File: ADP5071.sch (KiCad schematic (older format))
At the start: 29 parts, among them P7 PIN, P8 POUT, T1 NET-TIE, U4 ADP5071

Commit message: Latest power stuff
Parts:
- P7: footprint Pin_Headers:Pin_Header_Angled_1x02 -> Pin_Headers:Pin_Header_Straight_1x02
- P8: footprint Pin_Headers:Pin_Header_Angled_1x03 -> Pin_Headers:Pin_Header_Straight_1x03
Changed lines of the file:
@@
 F 0 "P7" H 2000 2900 50  0000 C CNN
 F 1 "PIN" V 2100 2750 50  0000 C CNN
-F 2 "Pin_Headers:Pin_Header_Angled_1x02" H 2000 2750 60  0001 C CNN
+F 2 "Pin_Headers:Pin_Header_Straight_1x02" H 2000 2750 60  0001 C CNN
 F 3 "" H 2000 2750 60  0000 C CNN
 	1    2000 2750
@@
 F 0 "P8" H 9800 3500 50  0000 C CNN
 F 1 "POUT" V 9900 3300 50  0000 C CNN
-F 2 "Pin_Headers:Pin_Header_Angled_1x03" H 9800 3300 60  0001 C CNN
+F 2 "Pin_Headers:Pin_Header_Straight_1x03" H 9800 3300 60  0001 C CNN
 F 3 "" H 9800 3300 60  0000 C CNN
 	1    9800 3300

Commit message: Latest work
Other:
- moved on the sheet: C19, C20, R8
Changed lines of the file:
@@
 L R R8
 U 1 1 56322611
-P 3700 3800
-F 0 "R8" V 3780 3800 50  0000 C CNN
-F 1 "5.23k" V 3600 3800 50  0000 C CNN
-F 2 "smd:SM0603" V 3630 3800 30  0001 C CNN
-F 3 "" H 3700 3800 30  0000 C CNN
-	1    3700 3800
+P 3700 3900
+F 0 "R8" V 3780 3900 50  0000 C CNN
+F 1 "5.23k" V 3600 3900 50  0000 C CNN
+F 2 "smd:SM0603" V 3630 3900 30  0001 C CNN
+F 3 "" H 3700 3900 30  0000 C CNN
+	1    3700 3900
 	-1   0    0    1
 $EndComp
@@
 L C C19
 U 1 1 56322618
-P 3700 4100
-F 0 "C19" H 3725 4200 50  0000 L CNN
-F 1 "8.2nF" H 3725 4000 50  0000 L CNN
-F 2 "smd:SM0603" H 3738 3950 30  0001 C CNN
-F 3 "" H 3700 4100 60  0000 C CNN
-	1    3700 4100
+P 3700 4200
+F 0 "C19" H 3725 4300 50  0000 L CNN
+F 1 "8.2nF" H 3725 4100 50  0000 L CNN
+F 2 "smd:SM0603" H 3738 4050 30  0001 C CNN
+F 3 "" H 3700 4200 60  0000 C CNN
+	1    3700 4200
 	1    0    0    -1
 $EndComp
@@
 L GND #PWR025
 U 1 1 5632261F
-P 3850 4250
-F 0 "#PWR025" H 3850 4000 50  0001 C CNN
-F 1 "GND" H 3850 4100 50  0000 C CNN
-F 2 "" H 3850 4250 60  0000 C CNN
-F 3 "" H 3850 4250 60  0000 C CNN
-	1    3850 4250
-	1    0    0    -1
-$EndComp
-Wire Wire Line
-	4300 3700 4700 3700
+P 3850 4350
+F 0 "#PWR025" H 3850 4100 50  0001 C CNN
+F 1 "GND" H 3850 4200 50  0000 C CNN
+F 2 "" H 3850 4350 60  0000 C CNN
+F 3 "" H 3850 4350 60  0000 C CNN
+	1    3850 4350
+	1    0    0    -1
+$EndComp
+Wire Wire Line
+	3700 3700 4700 3700
 Wire Wire Line
 	4700 3800 4500 3800
@@
 L C C20
 U 1 1 56322737
-P 4000 3950
-F 0 "C20" H 4025 4050 50  0000 L CNN
-F 1 "68pF" H 4025 3850 50  0000 L CNN
-F 2 "smd:SM0603" H 4038 3800 30  0001 C CNN
-F 3 "" H 4000 3950 60  0000 C CNN
-	1    4000 3950
-	1    0    0    -1
-$EndComp
-Wire Wire Line
-	3700 3650 3700 3600
-Wire Wire Line
-	3700 3600 4300 3600
-Wire Wire Line
-	4300 3600 4300 3700
-Wire Wire Line
-	4000 3800 4000 3600
-Connection ~ 4000 3600
-Wire Wire Line
-	3700 4250 4000 4250
-Wire Wire Line
-	4000 4250 4000 4100
-Connection ~ 3850 4250
+P 4000 4050
+F 0 "C20" H 4025 4150 50  0000 L CNN
+F 1 "68pF" H 4025 3950 50  0000 L CNN
+F 2 "smd:SM0603" H 4038 3900 30  0001 C CNN
+F 3 "" H 4000 4050 60  0000 C CNN
+	1    4000 4050
+	1    0    0    -1
+$EndComp
+Wire Wire Line
+	3700 3750 3700 3700
+Wire Wire Line
+	4000 3900 4000 3700
+Connection ~ 4000 3700
+Wire Wire Line
+	3700 4350 4000 4350
+Wire Wire Line
+	4000 4350 4000 4200
+Connection ~ 3850 4350
 $Comp
 L R R13

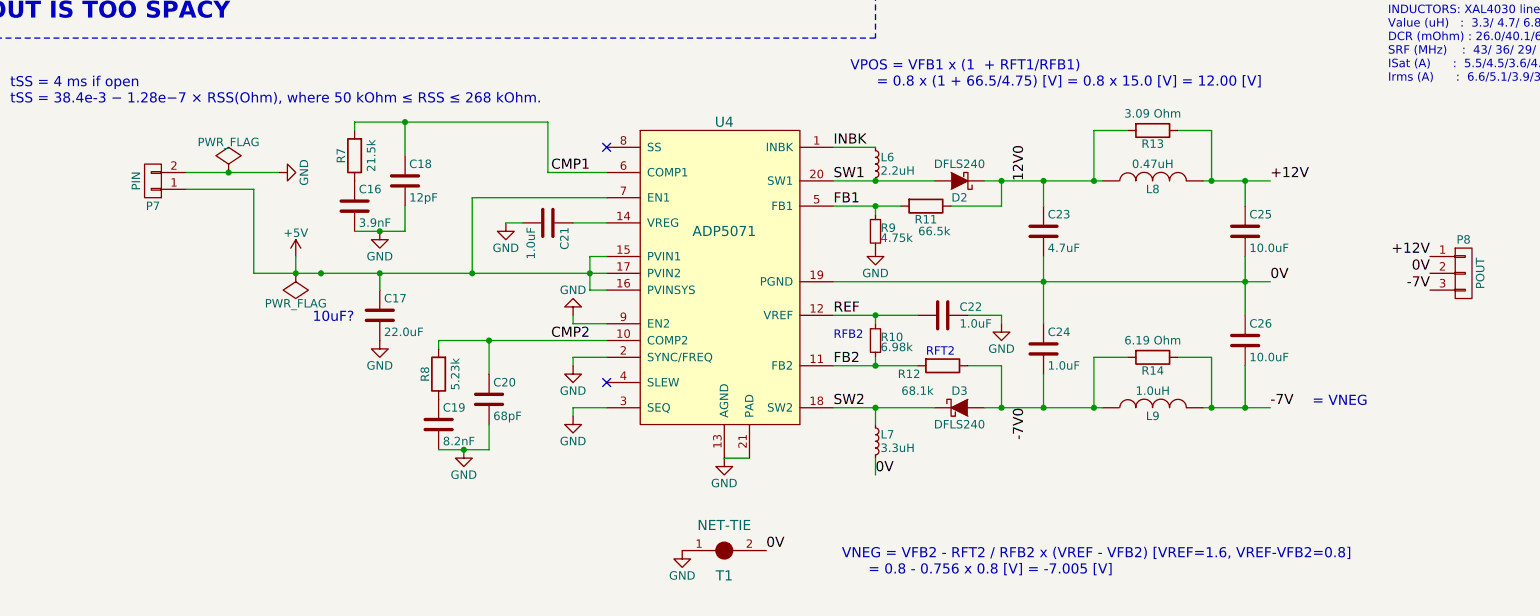
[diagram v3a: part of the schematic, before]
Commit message: Follow ADISimPower recommendations
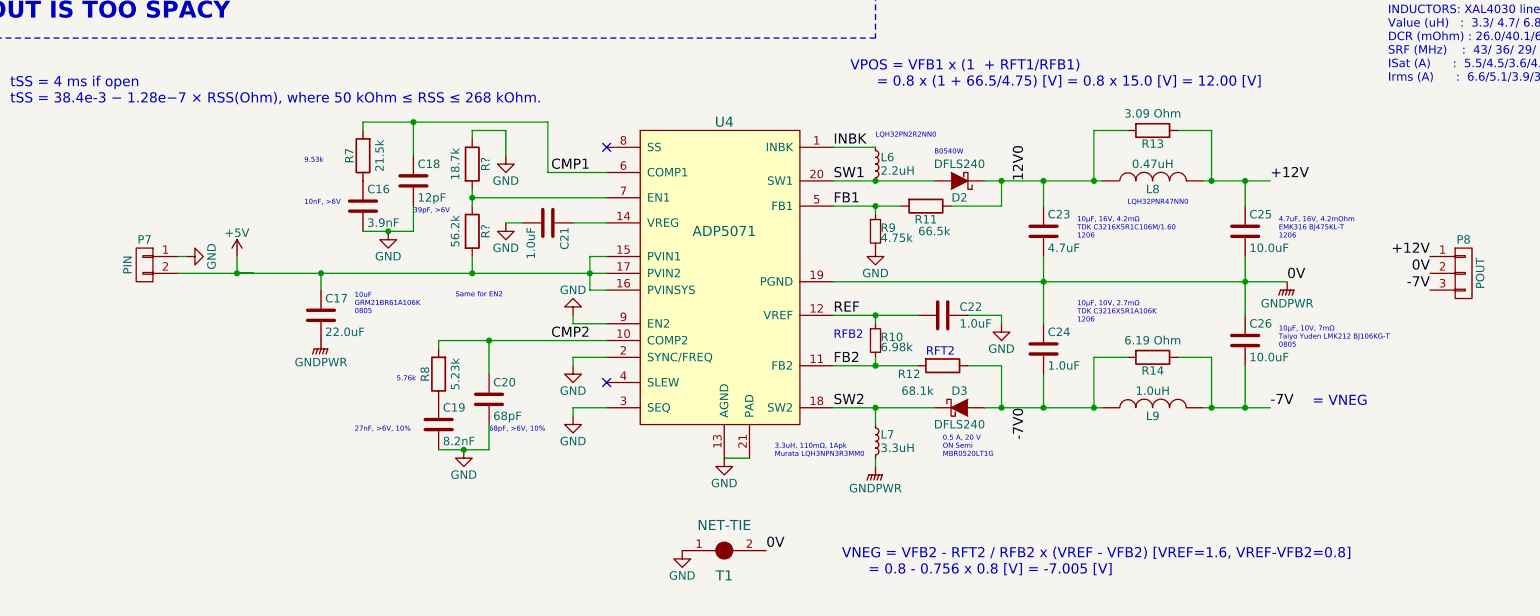
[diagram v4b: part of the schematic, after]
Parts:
- added R?: 56.2k, smd:SM0603, symbol R
- added R?: 18.7k, smd:SM0603, symbol R
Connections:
- net +5V: now also P7.2 (P2), R?.2; no longer P7.1 (P1), U4.7 (EN1)
- net GND: now also P7.1 (P1), R?.1; no longer C17.2, P7.2 (P2)
- net 0V renamed GNDPWR
- net GNDPWR: now also C17.2
- new net: R?.1, R?.2, U4.7 (EN1)
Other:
- note added: "0.5 A, 20 V\nON Semi \nMBR0520LT1G"
- note added: "10nF, >6V"
- note added: "10uF\nGRM21BR61A106K\n0805\n"
- note added: "10µF, 10V, 2.7mΩ\nTDK C3216X5R1A106K\n1206\n"
- note added: "10µF, 10V, 7mΩ\nTaiyo Yuden LMK212 BJ106KG-T\n0805"
- note added: "10µF, 16V, 4.2mΩ\nTDK C3216X5R1C106M/1.60\n1206"
- note added: "27nF, >6V, 10%"
- note added: "3.3uH, 110mΩ, 1Apk\nMurata LQH3NPN3R3MM0"
- note added: "39pF, >6V"
- note added: "4.7uF, 16V, 4.2mOhm\nEMK316 BJ475KL-T\n1206"
- note added: "5.76k"
- note added: "68pF, >6V, 10%"
- note added: "9.53k"
- note added: "B0540W"
- note added: "LQH32PN2R2NN0\n"
- note added: "LQH32PNR47NN0"
- note added: "Same for EN2"
- note removed: "10uF?\n"
- moved on the sheet: C16, C17, C18, P7, R7

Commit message: More work
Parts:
- L6: footprint engstad:inductor-smd-xal40 -> engstad:inductor-smd-1210
- L7: footprint SMD_Packages:SMD-1210_Pol -> engstad:inductor-smd-1212-lqh3np
- L8, L9: footprint SMD_Packages:SMD-1210_Pol -> engstad:inductor-smd-1210
- P7: footprint Pin_Headers:Pin_Header_Straight_1x02 -> xess:HDR_1x2
- P8: footprint Pin_Headers:Pin_Header_Straight_1x03 -> xess:HDR_1x3
- T1: footprint Oddities:NetTie-I_Connected_SMD -> engstad:net-tie-0.5mm
- U4: footprint Housings_DFN_QFN:QFN-20-1EP_4x4mm_Pitch0.5mm -> w_smd_qfn:pvqfn-n20
- gave numbers to parts that had none: 2

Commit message: Tiny fixes
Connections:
- net +5V renamed PWR_IN
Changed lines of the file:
@@
 $EndComp
 $Comp
-L GND #PWR023
+L GND #PWR026
 U 1 1 563225E0
 P 3400 3050
-F 0 "#PWR023" H 3400 2800 50  0001 C CNN
+F 0 "#PWR026" H 3400 2800 50  0001 C CNN
 F 1 "GND" H 3400 2900 50  0000 C CNN
 F 2 "" H 3400 3050 60  0000 C CNN
@@
 $EndComp
 $Comp
-L GND #PWR024
+L GND #PWR027
 U 1 1 563225EF
 P 4100 3000
-F 0 "#PWR024" H 4100 2750 50  0001 C CNN
+F 0 "#PWR027" H 4100 2750 50  0001 C CNN
 F 1 "GND" H 4100 2850 50  0000 C CNN
 F 2 "" H 4100 3000 60  0000 C CNN
@@
 $EndComp
 $Comp
-L +5V #PWR025
-U 1 1 5632260B
-P 2500 3200
-F 0 "#PWR025" H 2500 3050 50  0001 C CNN
-F 1 "+5V" H 2500 3340 50  0000 C CNN
-F 2 "" H 2500 3200 60  0000 C CNN
-F 3 "" H 2500 3200 60  0000 C CNN
-	1    2500 3200
-	1    0    0    -1
-$EndComp
-$Comp
 L R R8
 U 1 1 56322611
@@
 $EndComp
 $Comp
-L GND #PWR026
+L GND #PWR028
 U 1 1 5632261F
 P 3850 4350
-F 0 "#PWR026" H 3850 4100 50  0001 C CNN
+F 0 "#PWR028" H 3850 4100 50  0001 C CNN
 F 1 "GND" H 3850 4200 50  0000 C CNN
 F 2 "" H 3850 4350 60  0000 C CNN
@@
 $EndComp
 $Comp
-L GND #PWR027
+L GND #PWR029
 U 1 1 56322628
 P 4500 3850
-F 0 "#PWR027" H 4500 3600 50  0001 C CNN
+F 0 "#PWR029" H 4500 3600 50  0001 C CNN
 F 1 "GND" H 4500 3700 50  0000 C CNN
 F 2 "" H 4500 3850 60  0000 C CNN
@@
 $EndComp
 $Comp
-L GND #PWR028
+L GND #PWR030
 U 1 1 56322643
 P 6300 3150
-F 0 "#PWR028" H 6300 2900 50  0001 C CNN
+F 0 "#PWR030" H 6300 2900 50  0001 C CNN
 F 1 "GND" H 6300 3000 50  0000 C CNN
 F 2 "" H 6300 3150 60  0000 C CNN
@@
 $EndComp
 $Comp
-L GND #PWR029
+L GND #PWR031
 U 1 1 56322680
 P 5400 4400
-F 0 "#PWR029" H 5400 4150 50  0001 C CNN
+F 0 "#PWR031" H 5400 4150 50  0001 C CNN
 F 1 "GND" H 5400 4250 50  0000 C CNN
 F 2 "" H 5400 4400 60  0000 C CNN
@@
 $EndComp
 $Comp
-L GND #PWR030
+L GND #PWR032
 U 1 1 56322694
 P 7050 3600
-F 0 "#PWR030" H 7050 3350 50  0001 C CNN
+F 0 "#PWR032" H 7050 3350 50  0001 C CNN
 F 1 "GND" H 7050 3450 50  0000 C CNN
 F 2 "" H 7050 3600 60  0000 C CNN
@@
 $EndComp
 $Comp
-L GND #PWR031
+L GND #PWR033
 U 1 1 563226A9
 P 4500 3550
-F 0 "#PWR031" H 4500 3300 50  0001 C CNN
+F 0 "#PWR033" H 4500 3300 50  0001 C CNN
 F 1 "GND" H 4500 3400 50  0000 C CNN
 F 2 "" H 4500 3550 60  0000 C CNN
@@
 $EndComp
 $Comp
-L GND #PWR032
+L GND #PWR034
 U 1 1 563226B0
 P 4500 4150
-F 0 "#PWR032" H 4500 3900 50  0001 C CNN
+F 0 "#PWR034" H 4500 3900 50  0001 C CNN
 F 1 "GND" H 4500 4000 50  0000 C CNN
 F 2 "" H 4500 4150 60  0000 C CNN
@@
 $EndComp
 $Comp
-L GND #PWR033
+L GND #PWR035
 U 1 1 563226E2
 P 2200 3200
-F 0 "#PWR033" H 2200 2950 50  0001 C CNN
+F 0 "#PWR035" H 2200 2950 50  0001 C CNN
 F 1 "GND" H 2200 3050 50  0000 C CNN
 F 2 "" H 2200 3200 60  0000 C CNN
@@
 $EndComp
 $Comp
-L GND #PWR034
+L GND #PWR036
 U 1 1 563226F7
 P 5150 4950
-F 0 "#PWR034" H 5150 4700 50  0001 C CNN
+F 0 "#PWR036" H 5150 4700 50  0001 C CNN
 F 1 "GND" H 5150 4800 50  0000 C CNN
 F 2 "" H 5150 4950 60  0000 C CNN
@@
 -7V0
 $Comp
-L GNDPWR #PWR035
+L GNDPWR #PWR037
 U 1 1 565A09DD
 P 8750 3350
-F 0 "#PWR035" H 8750 3150 50  0001 C CNN
+F 0 "#PWR037" H 8750 3150 50  0001 C CNN
 F 1 "GNDPWR" H 8750 3220 50  0000 C CNN
 F 2 "" H 8750 3300 60  0000 C CNN
@@
 $EndComp
 $Comp
-L GNDPWR #PWR036
+L GNDPWR #PWR038
 U 1 1 565A0C5B
 P 6300 4450
-F 0 "#PWR036" H 6300 4250 50  0001 C CNN
+F 0 "#PWR038" H 6300 4250 50  0001 C CNN
 F 1 "GNDPWR" H 6300 4320 50  0000 C CNN
 F 2 "" H 6300 4400 60  0000 C CNN
@@
 $EndComp
 $Comp
-L GNDPWR #PWR037
+L GNDPWR #PWR039
 U 1 1 565A0F0B
 P 3000 3700
-F 0 "#PWR037" H 3000 3500 50  0001 C CNN
+F 0 "#PWR039" H 3000 3500 50  0001 C CNN
 F 1 "GNDPWR" H 3000 3570 50  0000 C CNN
 F 2 "" H 3000 3650 60  0000 C CNN
@@
 $EndComp
 $Comp
-L GND #PWR038
+L GND #PWR040
 U 1 1 565A3469
 P 4100 2600
-F 0 "#PWR038" H 4100 2350 50  0001 C CNN
+F 0 "#PWR040" H 4100 2350 50  0001 C CNN
 F 1 "GND" H 4100 2450 50  0000 C CNN
 F 2 "" H 4100 2600 60  0000 C CNN
@@
 Wire Notes Line
 	7750 5800 7750 6550
-Wire Wire Line
-	2500 3200 2500 3300
-Connection ~ 2500 3300
 Wire Wire Line
 	2150 3200 2200 3200
@@
 Wire Wire Line
 	2150 3300 4700 3300
+$Comp
+L PWR_FLAG #FLG041
+U 1 1 56760C54
+P 2700 3200
+F 0 "#FLG041" H 2700 3295 50  0001 C CNN
+F 1 "PWR_FLAG" H 2700 3424 50  0000 C CNN
+F 2 "" H 2700 3200 50  0000 C CNN
+F 3 "" H 2700 3200 50  0000 C CNN
+	1    2700 3200
+	1    0    0    -1
+$EndComp
+Wire Wire Line
+	2700 3200 2700 3300
+Connection ~ 2700 3300
+Text Label 3100 3300 0    60   ~ 0
+PWR_IN
 $EndSCHEMATC

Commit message: Safety checkin.
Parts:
- C16, C17, C18, C19, C20, C21, C22, C23, C24, C25, C26: symbol C -> Device:C
- D2, D3: symbol D_Schottky -> Device:D_Schottky
- L6, L7: symbol L_Small -> Device:L_Small
- L8: symbol INDUCTOR -> Device:L; Spice_Model (none) -> 0.47u; Spice_Netlist_Enabled (none) -> Y; Spice_Primitive (none) -> L
- L9: symbol INDUCTOR -> Device:L
- P7: symbol CONN_01X02 -> Connector_Generic:Conn_01x02
- P8: symbol CONN_01X03 -> Connector_Generic:Conn_01x03
- R10, R9: symbol R_Small -> Device:R_Small
- R11, R12, R35, R36, R8: symbol R -> Device:R
- R13: value 3.09 Ohm -> 3.09; symbol R -> Device:R; Spice_Model (none) -> 3.09; Spice_Netlist_Enabled (none) -> Y; Spice_Primitive (none) -> R
- R14: value 6.19 Ohm -> 6.19; symbol R -> Device:R; Spice_Model (none) -> 6.19; Spice_Netlist_Enabled (none) -> Y; Spice_Primitive (none) -> R
- R7: symbol R -> Device:R; Spice_Model (none) -> 21.5k; Spice_Netlist_Enabled (none) -> Y; Spice_Primitive (none) -> R
- T1: symbol NET-TIE -> Device:Net-Tie_2
- U4: symbol ADP5071 -> Engstad:ADP5071
